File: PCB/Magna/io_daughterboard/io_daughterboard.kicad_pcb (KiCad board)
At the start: 2 copper layers, 240 x 320 mm, 225 parts, among them J101 Conn_02x10_Counter_Clockwise, U201 74HC595, U202 74HC595, U203 74HC595, U204 74HC595, U205 74HC595, U301 XL9535, U501 NE5532, U502 4052, U601 NE5532, U602 4052, U701 NE5532, U702 4052

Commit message: Resize the IO PCB
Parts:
- moved J101 5.00 mm to (121.3, 292.0)
- moved RV408 5.00 mm to (85.0, 126.0)
- moved RV423 5.00 mm to (160.0, 126.0)
- moved C101 5.00 mm to (120.0, 295.0)
- moved C102 5.00 mm to (120.0, 266.0)
- moved C201 5.00 mm to (133.0, 248.0)
- moved C202 5.00 mm to (144.0, 181.5)
- moved C203 5.00 mm to (126.5, 181.5)
- moved C204 5.00 mm to (109.0, 181.5)
- moved C205 5.00 mm to (108.0, 233.0)
- moved C301 5.00 mm to (172.0, 245.0)
- moved C302 5.00 mm to (177.0, 229.0)
- moved C303 5.00 mm to (171.0, 269.0)
- moved C304 5.00 mm to (175.5, 227.0)
- moved C305 5.00 mm to (172.5, 267.0)
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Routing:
- net /Potentiometers/lsb: track 833.7 -> 822.2 mm
- net /Potentiometers/msb: track 814.7 -> 803.6 mm
- net /Potentiometers/ADC_4: track 633.4 -> 623.1 mm
- net /Potentiometers/ADC_5: track 661.7 -> 652.3 mm
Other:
- board size 240 x 320 mm -> 240 x 315 mm

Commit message: Start of redesign of Audio board
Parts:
- removed REF** (x2): JLC_toolinghole, JLC:JLC_toolinghole
- added H101: MountingHole_Pad, MountingHole:MountingHole_3.2mm_M3_Pad_Via, F.Cu at (226.0, 127.0)
- added H102: MountingHole_Pad, MountingHole:MountingHole_3.2mm_M3_Pad_Via, F.Cu at (160.0, 107.0)
- added H103: MountingHole_Pad, MountingHole:MountingHole_3.2mm_M3_Pad_Via, F.Cu at (131.0, 25.0)
- added H104: MountingHole_Pad, MountingHole:MountingHole_3.2mm_M3_Pad_Via, F.Cu at (232.0, 32.0)
- C101, C102: value 1uF/50V -> 22uF/25V
- C201, C202, C203, C204, C205, C301, C302, C303, C304, C305, C306, C307, C308, C309, C310, C311, C312, C313, C314, C315, C316, C317, C501, C502, C601, C602, C701, C702: value 100nF/50V -> 22uF/25V
- RV401, RV402, RV403, RV404, RV405, RV406, RV413, RV414, RV416, RV417, RV421: value 10k/PTV09A-4020F-B103 -> 10k/PTV09A-4030F-B103
- RV407, RV408, RV410, RV411, RV412, RV418, RV419, RV420, RV422, RV423: value 10k/PTV09A-4220F-B103 -> 10k/PTV09A-4230F-B103
- RV415: value 10k/PTV09A-4020F-B103 -> 10k/PTV09A-2030F-B103; footprint Potentiometer_THT:Potentiometer_Bourns_PTV09A-1_Single_Vertical -> Potentiometer_THT:Potentiometer_Bourns_PTV09A-2_Single_Horizontal
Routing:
- net VDDA: track 1777.1 -> 1779.2 mm
- net /Potentiometers/lsb: track 822.2 -> 823.1 mm

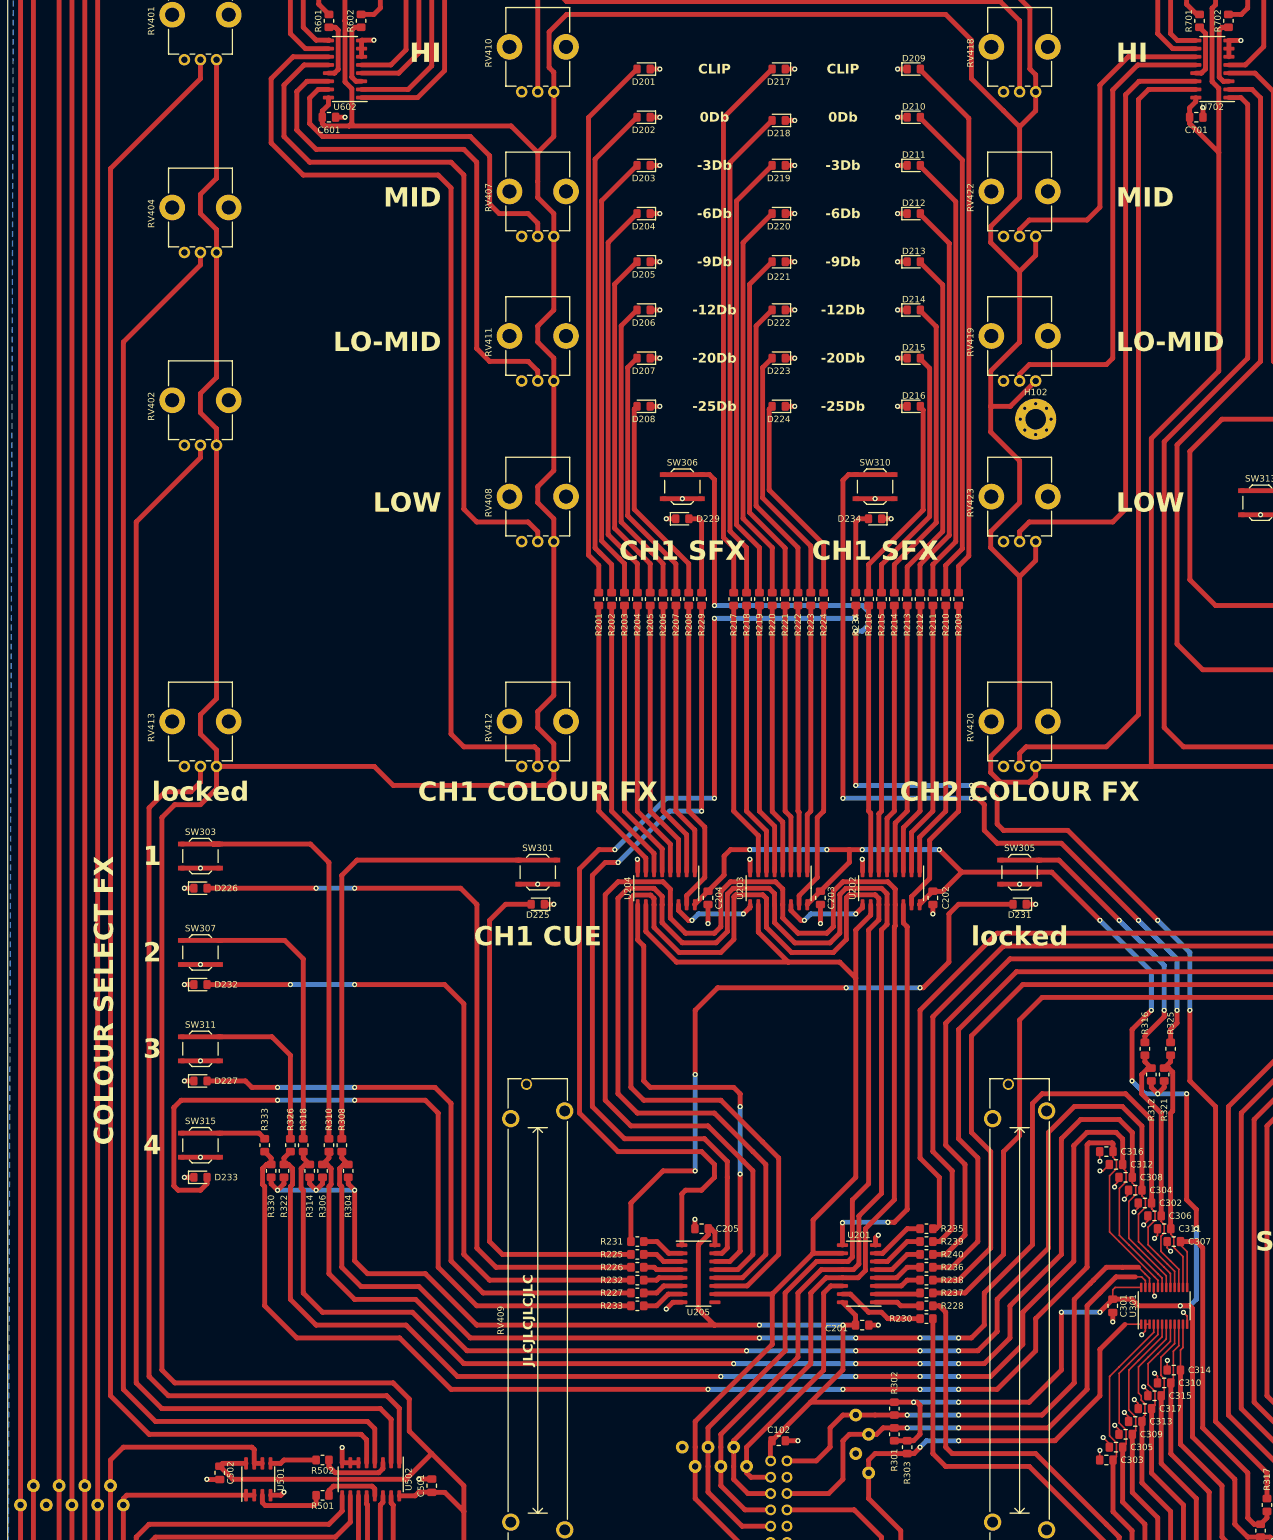
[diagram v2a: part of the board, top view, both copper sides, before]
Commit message: Update some files to KiCad8 and make ready for production
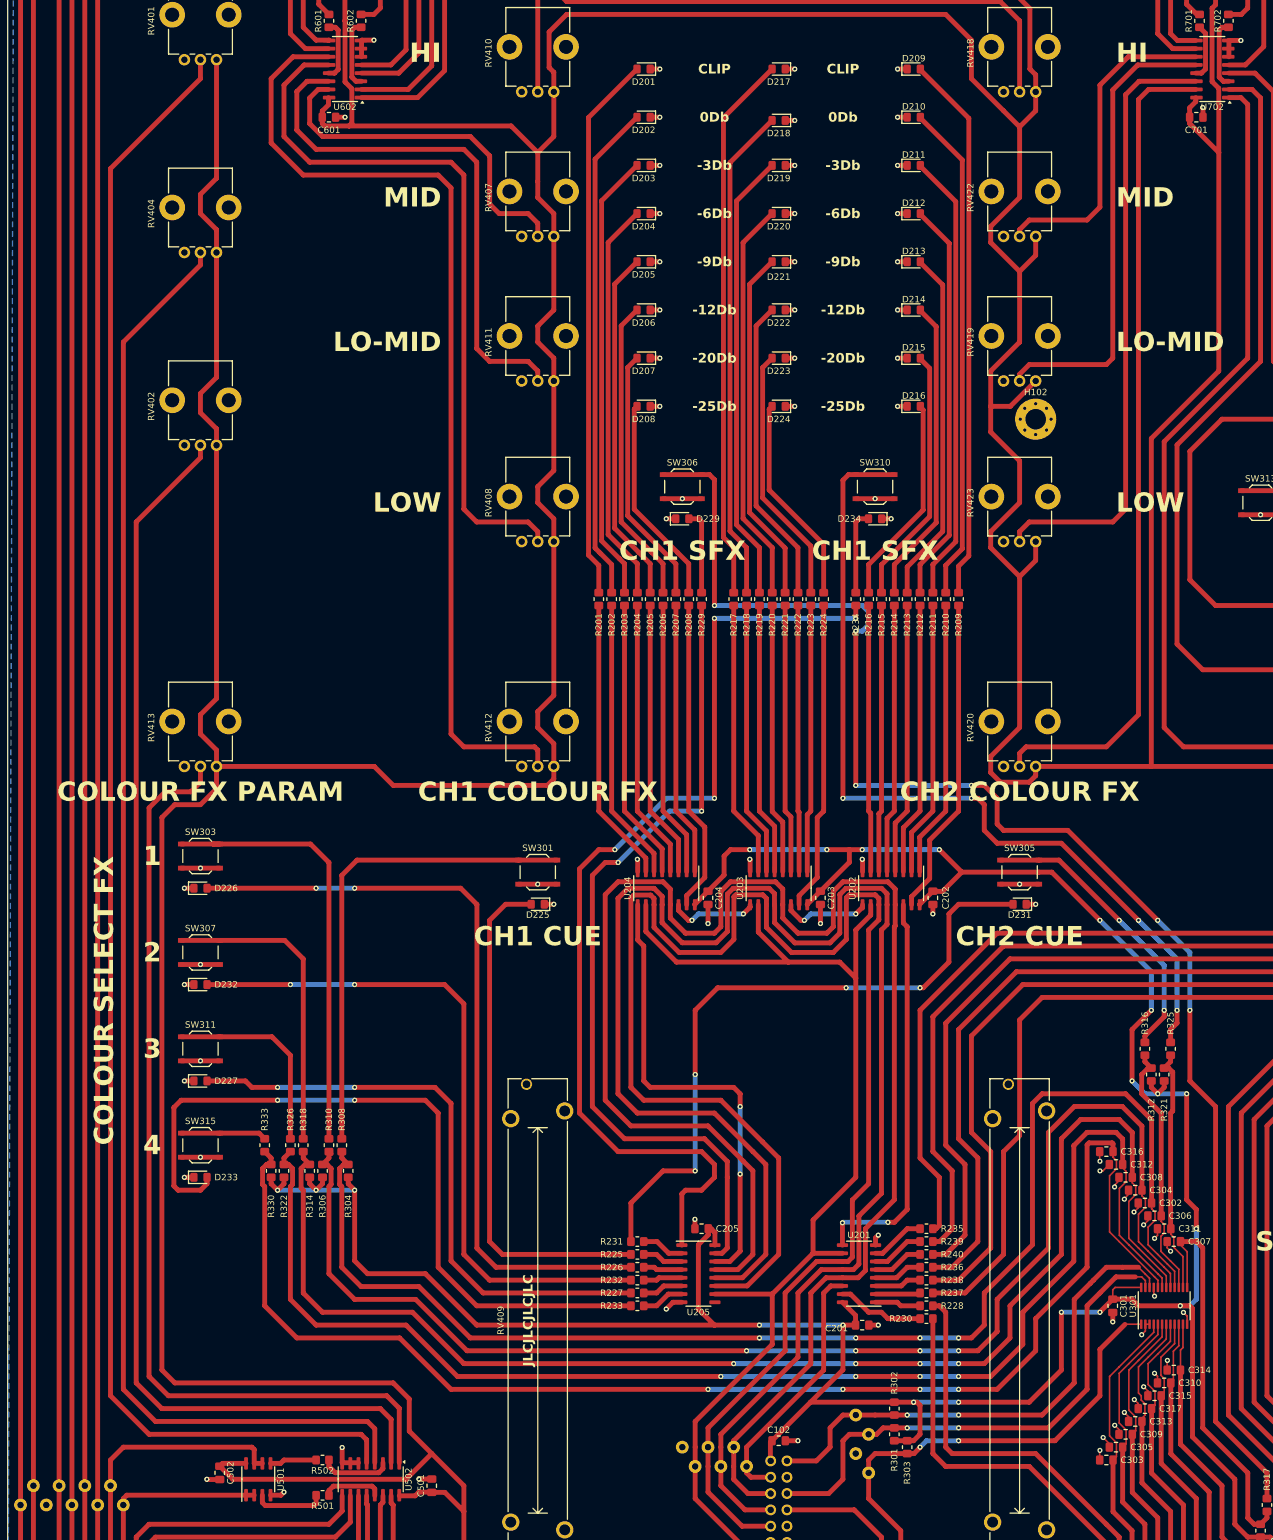
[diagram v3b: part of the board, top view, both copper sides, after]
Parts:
- U502, U602, U702: footprint Package_SO:SO-16_3.9x9.9mm_P1.27mm -> Package_SO:SOIC-16_3.9x9.9mm_P1.27mm
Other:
- board text added: "CH2 CUE"
- board text added: "COLOUR FX PARAM"
- board text removed: "locked"

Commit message: Update Project to Kicad 8.0 and prepare for production
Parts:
- RV401, RV402, RV403, RV404, RV405, RV406, RV413, RV414, RV416, RV417, RV421: value 10k/PTV09A-4030F-B103 -> 10k/PTV09A-4030F-B103
- RV407, RV408, RV410, RV411, RV412, RV418, RV419, RV420, RV422, RV423: value 10k/PTV09A-4230F-B103 -> 10k/PTV09A-4230F-B103
- RV409, RV424: value 10k/ PTA6043-2015DPB103 -> 10k/ PTA6043-2015DPB103
- RV415: moved to B.Cu
- moved RV415 0.05 mm to (32.5, 296.0), turned to -90 degrees
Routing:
- net Net-(D235-A): track 312.4 -> 311.3 mm
- net Net-(D238-A): track 272.2 -> 271.4 mm
- net Net-(D236-A): track 282.1 -> 281.3 mm
- net Net-(D240-A): track 291.4 -> 290.6 mm
- net Net-(D239-A): track 302.3 -> 301.4 mm

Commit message: Fix some more small issues on IO board
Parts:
- added H105: MountingHole_Pad, MountingHole:MountingHole_3.2mm_M3_Pad_Via, F.Cu at (24.3, 141.7)
- added H106: MountingHole_Pad, MountingHole:MountingHole_3.2mm_M3_Pad_Via, F.Cu at (80.0, 140.0)
- added H107: MountingHole_Pad, MountingHole:MountingHole_3.2mm_M3_Pad_Via, F.Cu at (95.0, 25.0)
- added H108: MountingHole_Pad, MountingHole:MountingHole_3.2mm_M3_Pad_Via, F.Cu at (15.0, 15.0)
- added H109: MountingHole_Pad, MountingHole:MountingHole_3.2mm_M3_Pad_Via, F.Cu at (45.0, 290.0)
- added H110: MountingHole_Pad, MountingHole:MountingHole_3.2mm_M3_Pad_Via, F.Cu at (70.0, 262.5)
